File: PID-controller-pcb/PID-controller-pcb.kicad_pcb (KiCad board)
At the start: 2 copper layers, 165.4 x 86 mm, 12 parts, among them SW1 PinHeader_1x03_P2.54mm_Vertic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

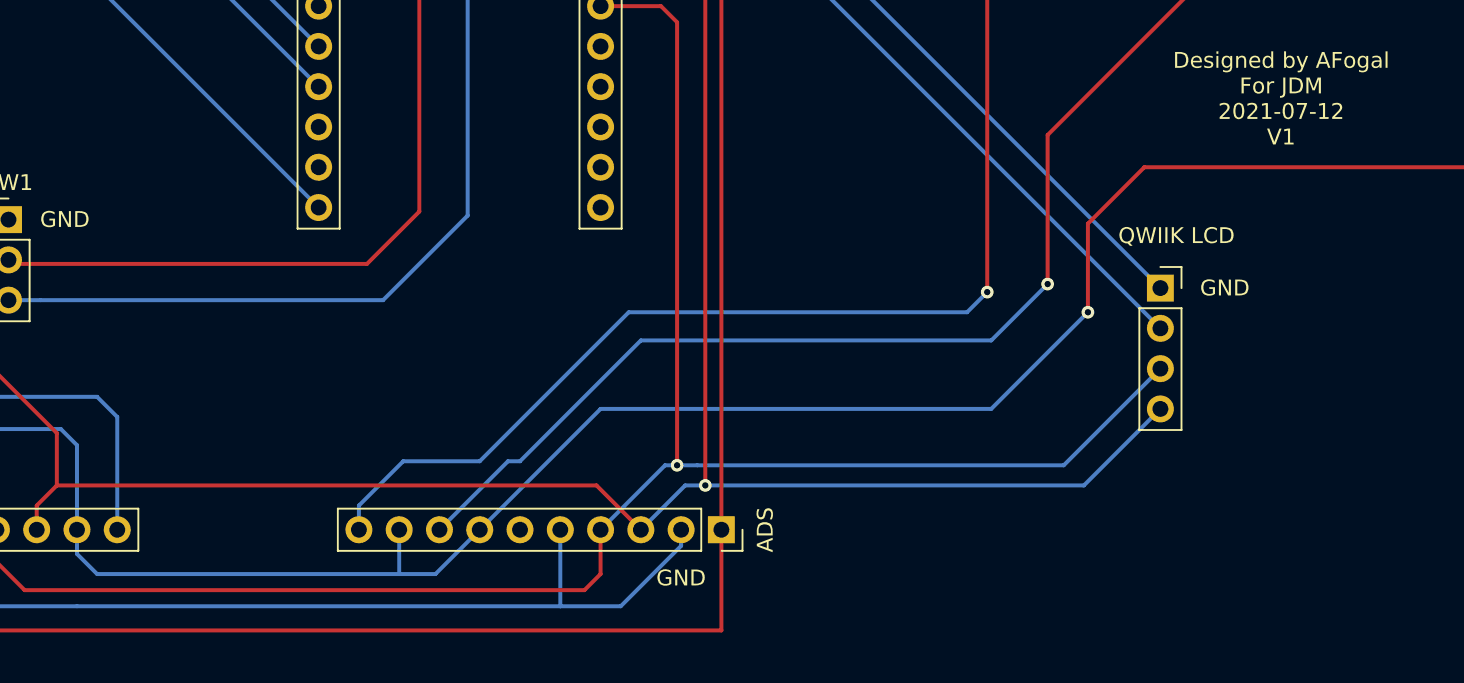
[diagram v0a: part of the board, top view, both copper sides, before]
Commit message: Tweaked pcb to make version 2 with fixed grounding and correctly oriented differentials
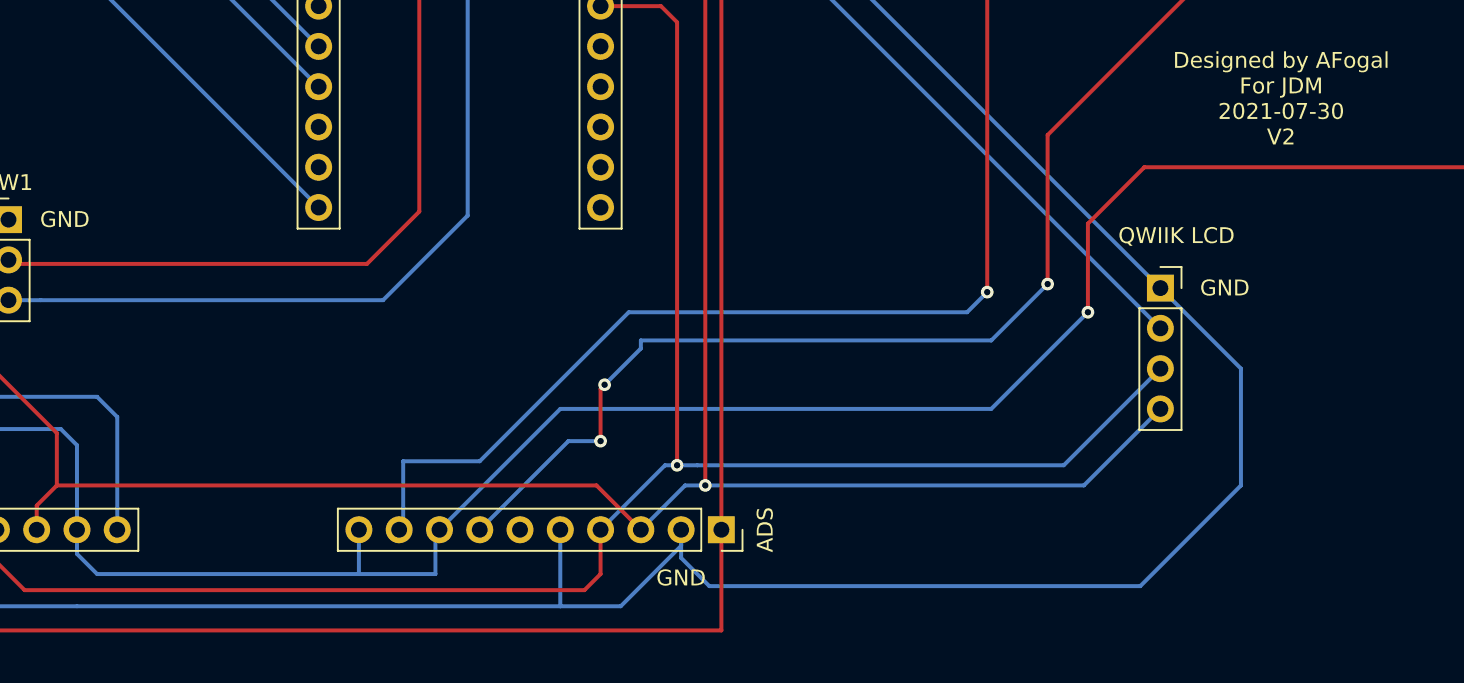
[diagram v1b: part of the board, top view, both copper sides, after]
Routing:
- net (no net): track 2126.1 -> 2181.2 mm, vias 9 -> 11
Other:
- board text added: "Designed by AFogal For JDM 2021-07-30 V2"
- board text removed: "Designed by AFogal For JDM 2021-07-12 V1"

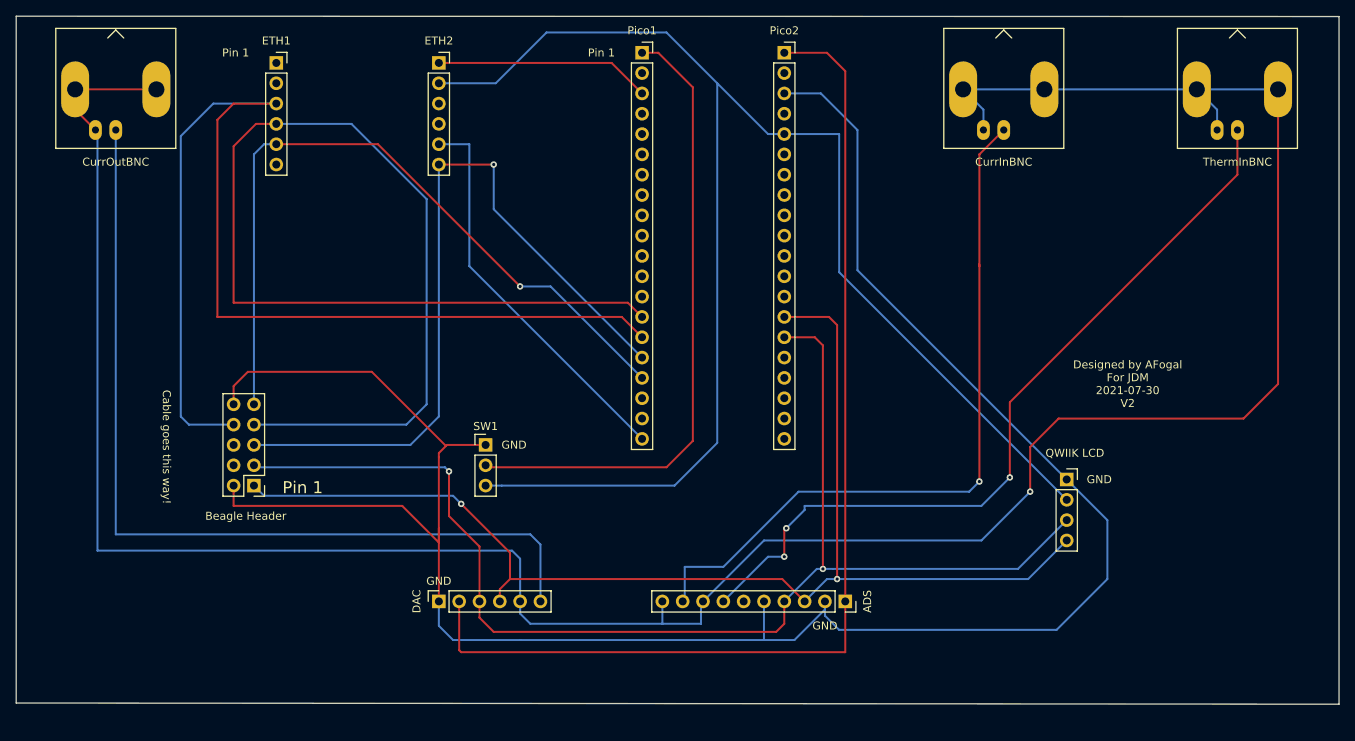
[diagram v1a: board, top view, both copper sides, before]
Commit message: Redesigned board for PoE
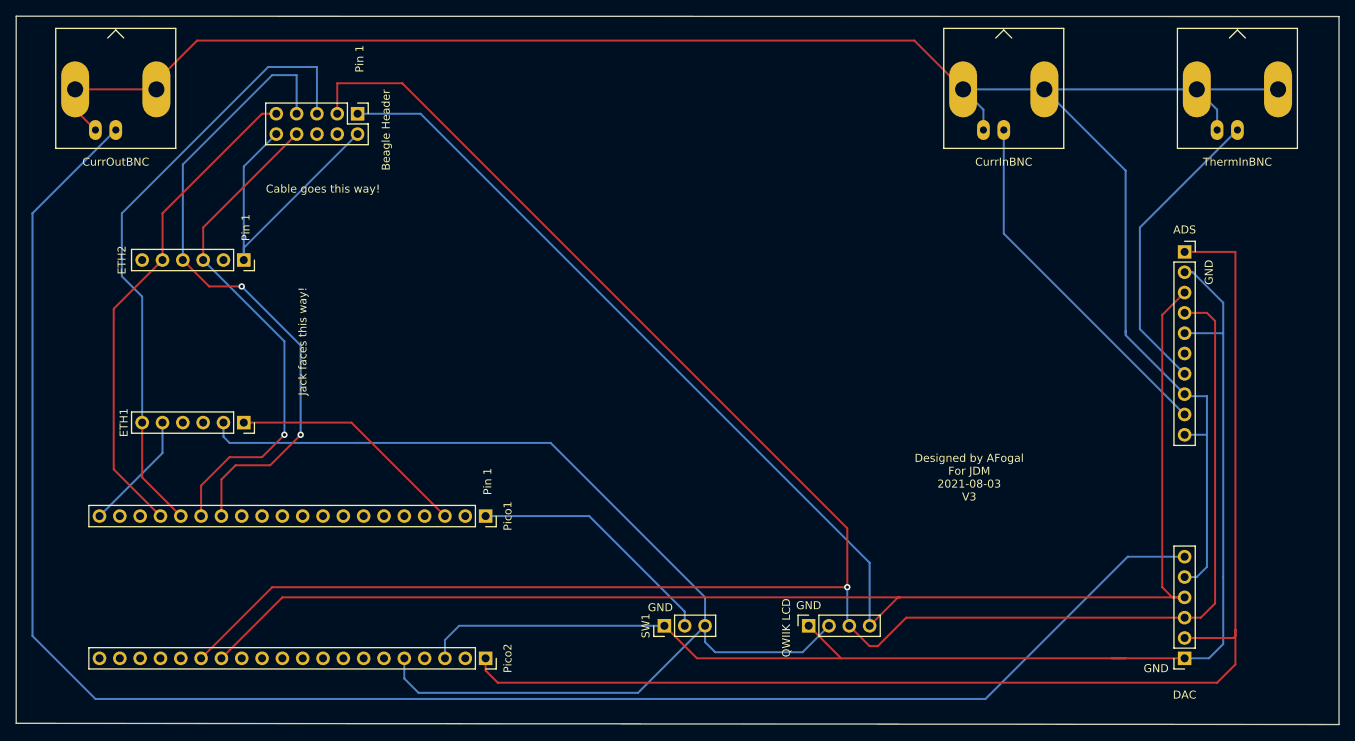
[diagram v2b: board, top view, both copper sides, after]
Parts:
- moved DAC 93.5 mm to (249.4, 125.2), turned to 180 degrees
- moved Pico2 84.4 mm to (162.1, 125.2), turned to 270 degrees
- moved Pico1 61.1 mm to (162.1, 107.4), turned to 270 degrees
- moved ADS 60.9 mm to (249.4, 74.4), turned to 0 degrees
- moved Beagle Header 48.3 mm to (146.1, 57.1), turned to 270 degrees
- moved ETH1 45.1 mm to (131.8, 95.8), turned to 270 degrees
- moved QWIIK LCD 37.1 mm to (202.4, 121.2), turned to 90 degrees
- moved ETH2 34.7 mm to (131.8, 75.4), turned to 270 degrees
- moved SW1 31.8 mm to (184.4, 121.2), turned to 90 degrees
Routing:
- net (no net): track 2181.2 -> 1964.3 mm, vias 11 -> 4
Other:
- board size 165.4 x 86 mm -> 165.4 x 88.5 mm
- board text added: "Designed by AFogal For JDM 2021-08-03 V3"
- board text added: "Jack faces this way!"
- board text removed: "Designed by AFogal For JDM 2021-07-30 V2"
